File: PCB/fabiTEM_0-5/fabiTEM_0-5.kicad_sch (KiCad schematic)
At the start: 79 parts, among them J1 USB_C_Receptacle, J2 USB_C_Receptacle, U1 rp2040-zero

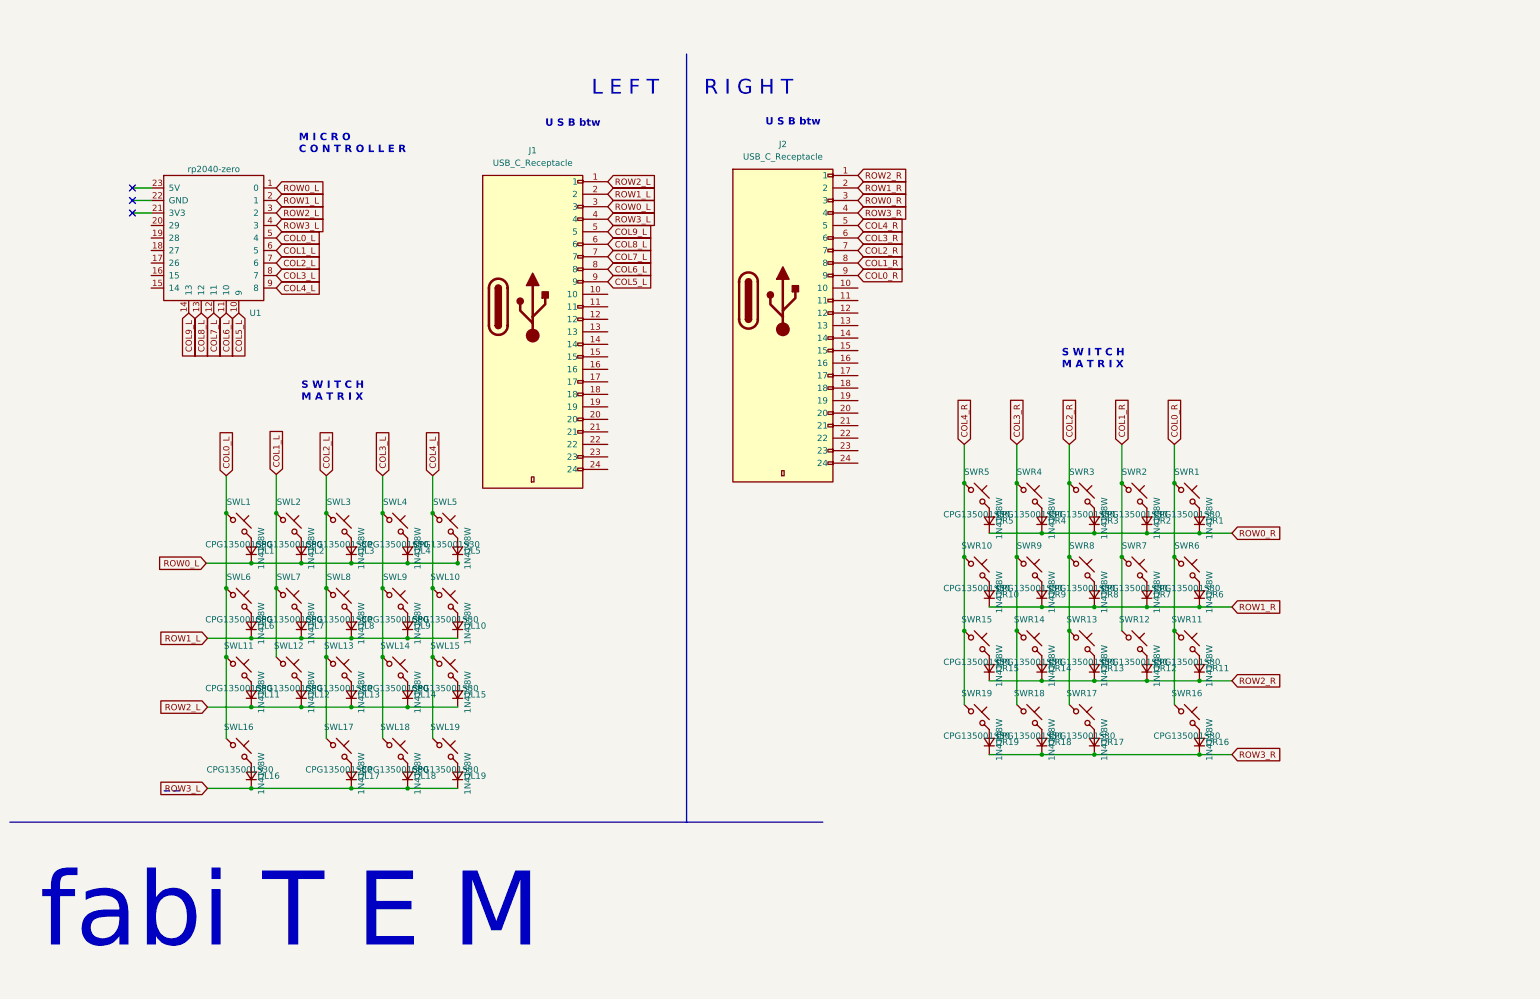
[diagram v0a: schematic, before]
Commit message: Rewiring of the entire thing, triple USB-C, IO expander
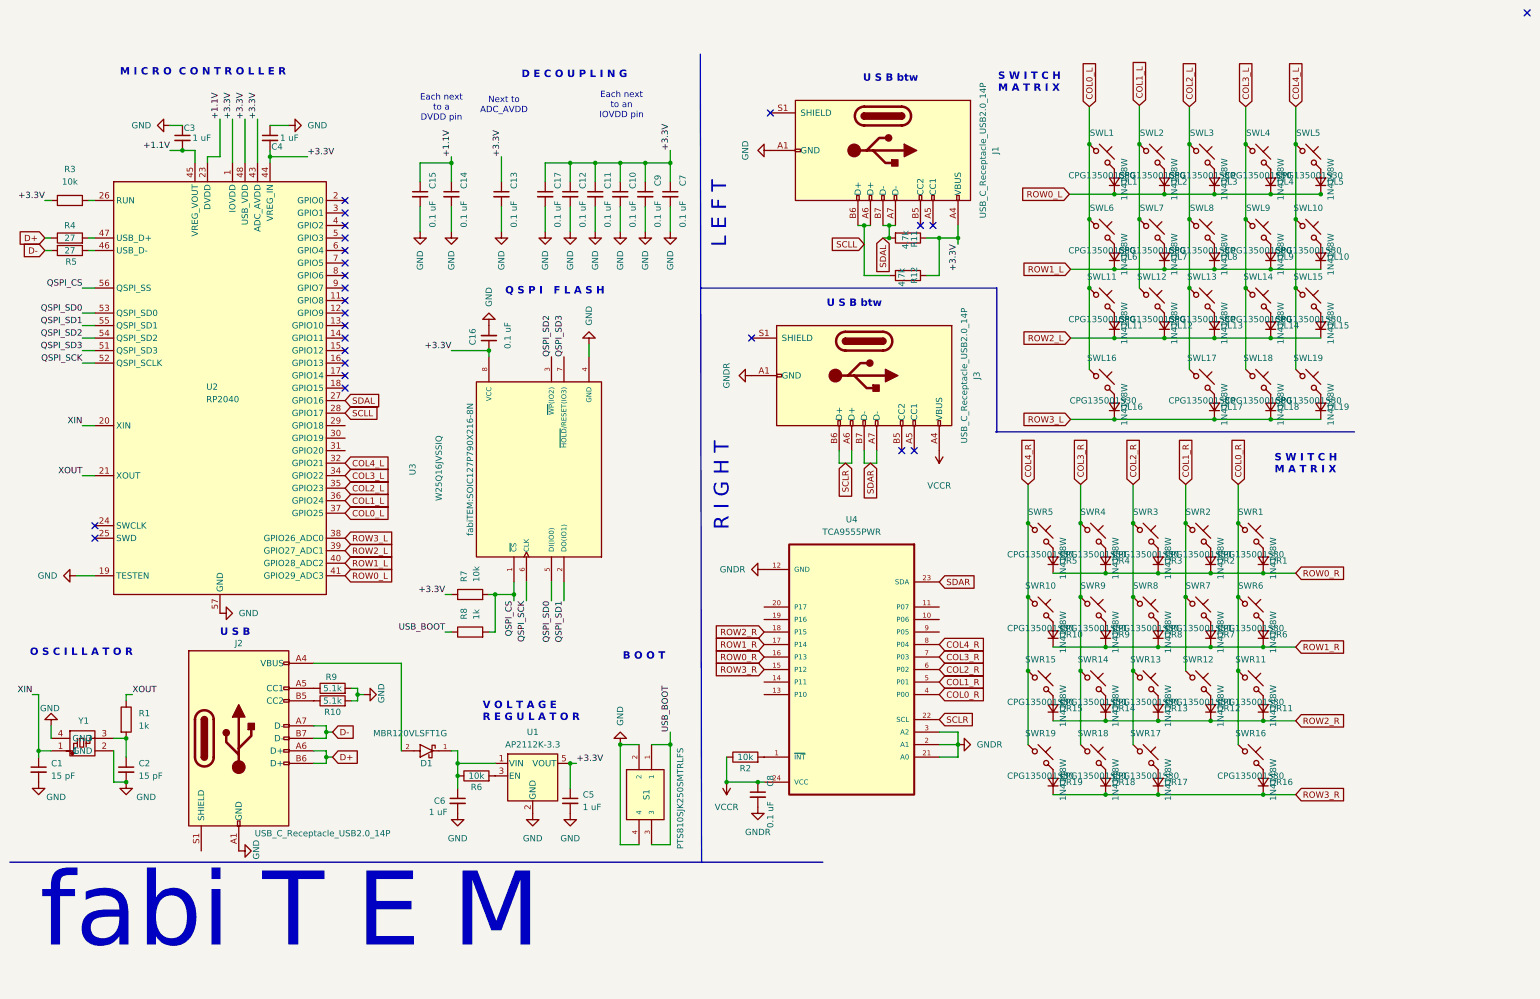
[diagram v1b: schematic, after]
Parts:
- removed J1, J2: USB_C_Receptacle, fabiTEM:USB-C-SMD_GT-USB-7013, symbol fabiTEM:USB_C_Receptacle
- removed U1: rp2040-zero, mcu:rp2040-zero-tht, symbol mcu:rp2040-zero
- added C1, C2: 15 pF, Capacitor_SMD:C_0201_0603Metric, symbol Device:C_Small
- added C10, C11, C12, C13, C14, C15, C16, C17, C7, C8, C9: 0.1 uF, Capacitor_SMD:C_0201_0603Metric, symbol Device:C_Small
- added C3, C4, C5, C6: 1 uF, Capacitor_SMD:C_0201_0603Metric, symbol Device:C_Small
- added D1: MBR120VLSFT1G, fabiTEM:DIOM3616X98N, symbol MBR120VLSFT1G:MBR120VLSFT1G
- added J1, J2, J3: USB_C_Receptacle_USB2.0_14P, fabiTEM:USB_C_Receptacle_GCT_USB4105-xx-A_16P_TopMnt_Horizontal, symbol fabiTEM:USB_C_Receptacle_USB2.0_14P
- added R1, R8: 1k, Resistor_SMD:R_0201_0603Metric, symbol Device:R
- added R10, R9: 5.1k, Resistor_SMD:R_0201_0603Metric, symbol Device:R
- added R11, R12: 4.7k, Resistor_SMD:R_0201_0603Metric, symbol Device:R
- added R2, R3, R6, R7: 10k, Resistor_SMD:R_0201_0603Metric, symbol Device:R
- added R4, R5: 27, Resistor_SMD:R_0201_0603Metric, symbol Device:R
- added S1: PTS810SJK250SMTRLFS, fabiTEM:PTS810SJG250SMTRLFS, symbol PTS810SJK250SMTRLFS:PTS810SJK250SMTRLFS
- added U1: AP2112K-3.3, Package_TO_SOT_SMD:SOT-23-5, symbol Regulator_Linear:AP2112K-3.3
- added U2: RP2040, Package_DFN_QFN:QFN-56-1EP_7x7mm_P0.4mm_EP3.2x3.2mm, symbol MCU_RaspberryPi:RP2040
- added U3: W25Q16JVSSIQ, fabiTEM:SOIC127P790X216-8N, symbol W25Q16JVSSIQ:W25Q16JVSSIQ
- added U4: TCA9555PWR, fabiTEM:SOP65P640X120-24N, symbol TCA9555PWR:TCA9555PWR
- added Y1: ~, fabiTEM:ABM8-272-T3, symbol fabiTEM:ABM8-272-T3
- SWL1, SWL10, SWL11, SWL12, SWL13, SWL14, SWL15, SWL16, SWL17, SWL18, SWL19, SWL2, SWL3, SWL4, SWL5, SWL6, SWL7, SWL8, SWL9, SWR1, SWR10, SWR11, SWR12, SWR13, SWR14, SWR15, SWR16, SWR17, SWR18, SWR19, SWR2, SWR3, SWR4, SWR5, SWR6, SWR7, SWR8, SWR9: footprint TOTEMlib:Kailh_socket_PG1350_optional -> fabiTEM:Kailh_socket_PG1350_reverse
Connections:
- net COL0_L: now also U2.37 (GPIO25)
- net COL0_R: now also U4.4 (P00)
- net COL1_L: now also U2.36 (GPIO24)
- net COL1_R: now also U4.5 (P01)
- net COL2_L: now also U2.35 (GPIO23)
- net COL2_R: now also U4.6 (P02)
- net COL3_L: now also U2.34 (GPIO22)
- net COL3_R: now also U4.7 (P03)
- net COL4_L: now also U2.32 (GPIO21)
- net COL4_R: now also U4.8 (P04)
- net ROW0_L: now also U2.41 (GPIO29_ADC3)
- net ROW0_R: now also U4.16 (P13)
- net ROW1_L: now also U2.40 (GPIO28_ADC2)
- net ROW1_R: now also U4.17 (P14)
- net ROW2_L: now also U2.39 (GPIO27_ADC1)
- net ROW2_R: now also U4.18 (P15)
- net ROW3_L: now also U2.38 (GPIO26_ADC0)
- net ROW3_R: now also U4.15 (P12)
- new net: J2.B5 (CC2), R10.1
- new net: J2.A5 (CC1), R9.1
- new net: R2.2, U4.1 (~{INT})
- new net: C2.1, R1.2, Y1.3
- new net: C6.1, D1.1, R6.1, U1.1 (VIN)
- new net: D1.2, J2.A4 (VBUS), J2.A9 (VBUS), J2.B4 (VBUS), J2.B9 (VBUS)
- new net: R3.2, U2.26 (RUN)
- new net: R6.2, U1.3 (EN)
- new net: R4.2, U2.47 (USB_D+)
- new net: R5.1, U2.46 (USB_D-)
- new net +1.1V: C14.1, C15.1, C3.2, U2.23 (DVDD), U2.45 (VREG_VOUT), U2.50 (DVDD)
- new net +3.3V: C10.1, C11.1, C12.1, C13.1, C16.1, C17.1, C4.2, C5.1, C7.1, C9.1, J1.A4 (VBUS), J1.A9 (VBUS), J1.B4 (VBUS), J1.B9 (VBUS), R11.1, R12.1, R3.1, R7.1, U1.5 (VOUT), U2.1 (IOVDD), U2.10 (IOVDD), U2.22 (IOVDD), U2.33 (IOVDD), U2.42 (IOVDD), U2.43 (ADC_AVDD), U2.44 (VREG_IN), U2.48 (USB_VDD), U2.49 (IOVDD), U3.8 (VCC)
- new net D+: J2.A6 (D+), J2.B6 (D+), R4.1
- new net D-: J2.A7 (D-), J2.B7 (D-), R5.2
- new net GND: C1.2, C10.2, C11.2, C12.2, C13.2, C14.2, C15.2, C16.2, C17.2, C2.2, C3.1, C4.1, C5.2, C6.2, C7.2, C9.2, J1.A1 (GND), J1.A12 (GND), J1.B1 (GND), J1.B12 (GND), J2.A1 (GND), J2.A12 (GND), J2.B1 (GND), J2.B12 (GND), R10.2, R9.2, S1.2, S1.4, U1.2 (GND), U2.19 (TESTEN), U2.57 (GND), U3.4 (GND), Y1.2 (GND), Y1.4 (GND)
- new net GNDR: C8.2, J3.A1 (GND), J3.A12 (GND), J3.B1 (GND), J3.B12 (GND), U4.12 (GND), U4.2 (A1), U4.21 (A0), U4.3 (A2)
- new net QSPI_CS: R7.2, R8.2, U2.56 (QSPI_SS), U3.1 (~{CS})
- new net QSPI_SCK: U2.52 (QSPI_SCLK), U3.6 (CLK)
- new net QSPI_SD0: U2.53 (QSPI_SD0), U3.5 (DI(IO0))
- new net QSPI_SD1: U2.55 (QSPI_SD1), U3.2 (DO(IO1))
- new net QSPI_SD2: U2.54 (QSPI_SD2), U3.3 (~{WP}(IO2))
- new net QSPI_SD3: U2.51 (QSPI_SD3), U3.7 (~{HOLD}/RESET(IO3))
- new net SCLL: J1.A6 (D+), J1.B6 (D+), R12.2, U2.28 (GPIO17)
- new net SCLR: J3.A6 (D+), J3.B6 (D+), U4.22 (SCL)
- new net SDAL: J1.A7 (D-), J1.B7 (D-), R11.2, U2.27 (GPIO16)
- new net SDAR: J3.A7 (D-), J3.B7 (D-), U4.23 (SDA)
- new net USB_BOOT: R8.1, S1.1, S1.3
- new net VCCR: C8.1, J3.A4 (VBUS), J3.A9 (VBUS), J3.B4 (VBUS), J3.B9 (VBUS), R2.1, U4.24 (VCC)
- new net XIN: C1.1, U2.20 (XIN), Y1.1
- new net XOUT: R1.1, U2.21 (XOUT)
- no-connect marks 3 -> 25
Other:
- note added: "B O O T"
- note added: "D E C O U P L I N G"
- note added: "Each next to a DVDD pin"
- note added: "Each next to an IOVDD pin"
- note added: "Next to ADC_AVDD"
- note added: "O S C I L L A T O R"
- note added: "Q S P I F L A S H"
- note added: "U S B"
- note added: "V O L T A G E R E G U L A T O R"
- moved on the sheet: DL1, DL10, DL11, DL12, DL13, DL14, DL15, DL16, DL17, DL18, DL19, DL2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

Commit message: adafruit io expander
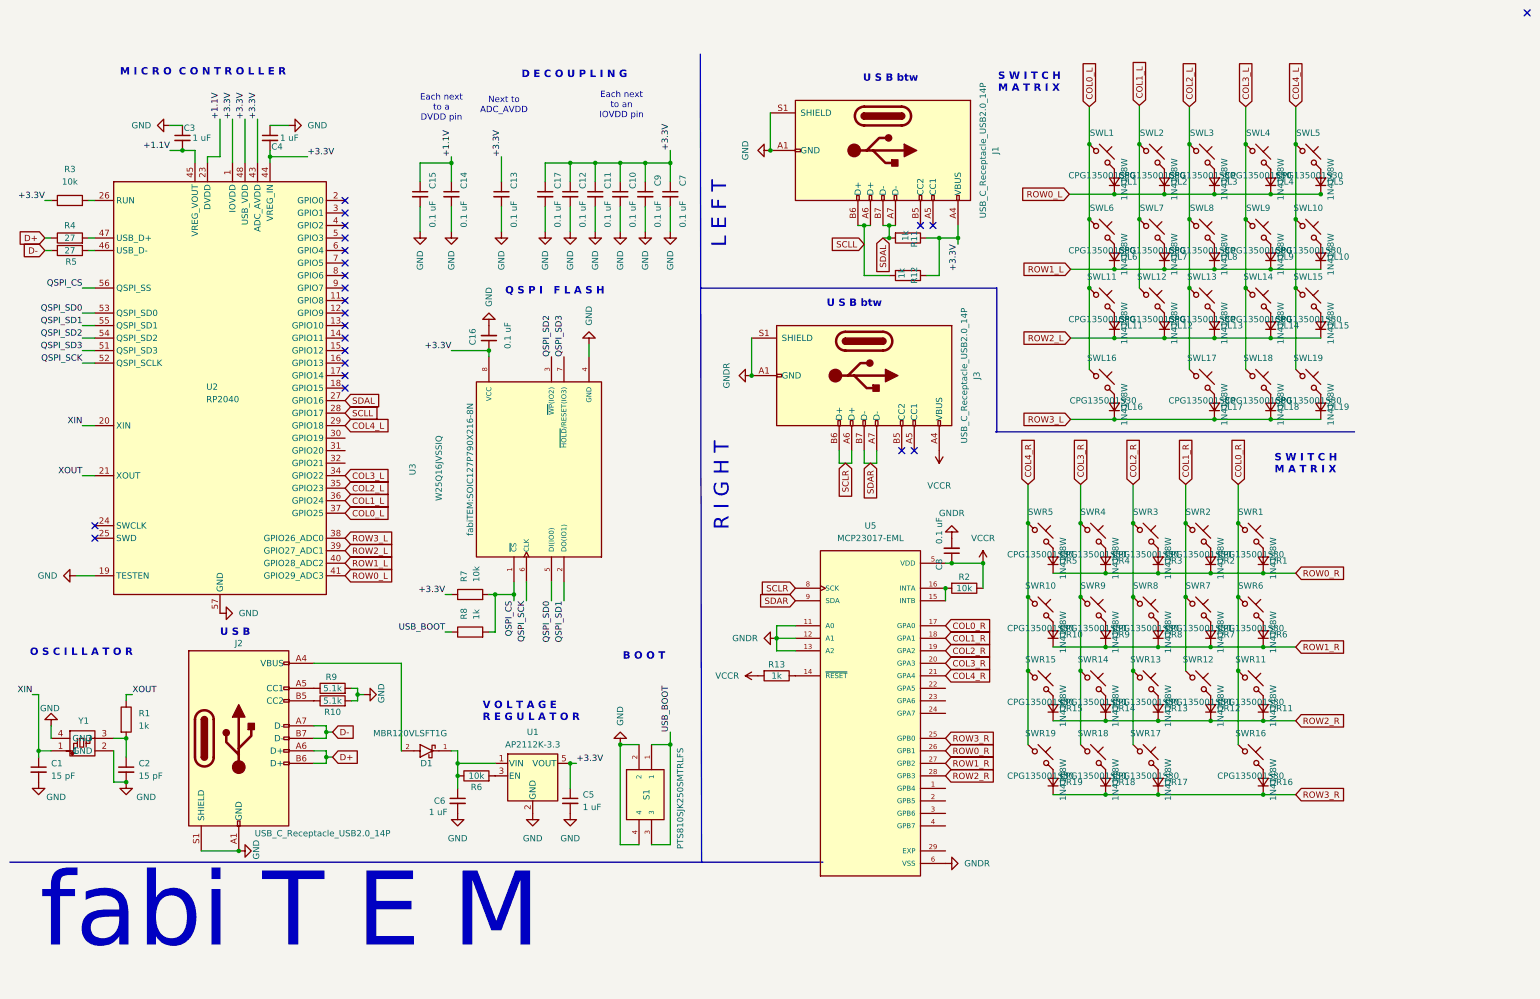
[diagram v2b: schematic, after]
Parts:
- removed U4: TCA9555PWR, fabiTEM:SOP65P640X120-24N, symbol TCA9555PWR:TCA9555PWR
- added R13: 1k, Resistor_SMD:R_0201_0603Metric, symbol Device:R
- added U5: MCP23017-EML, fabiTEM:QFN65P600X600X100-29N, symbol MCP23017-EML:MCP23017-EML
- R11, R12: value 4.7k -> 1k
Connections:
- net COL0_R: now also U5.17 (GPA0)
- net COL1_R: now also U5.18 (GPA1)
- net COL2_R: now also U5.19 (GPA2)
- net COL3_R: now also U5.20 (GPA3)
- net COL4_L: now also U2.29 (GPIO18); no longer U2.32 (GPIO21)
- net COL4_R: now also U5.21 (GPA4)
- net GND: now also J1.S1 (SHIELD), J2.S1 (SHIELD)
- net GNDR: now also J3.S1 (SHIELD), U5.11 (A0), U5.12 (A1), U5.13 (A2), U5.6 (VSS)
- net ROW0_R: now also U5.26 (GPB1)
- net ROW1_R: now also U5.27 (GPB2)
- net ROW2_R: now also U5.28 (GPB3)
- net ROW3_R: now also U5.25 (GPB0)
- net SCLR: now also U5.8 (SCK)
- net SDAR: now also U5.9 (SDA)
- net VCCR: now also R13.2, U5.5 (VDD)
- net at R2.2: now also U5.15 (INTB), U5.16 (INTA)
- new net: R13.1, U5.14 (~{RESET})
- no-connect marks 25 -> 23
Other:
- moved on the sheet: C8, R2
